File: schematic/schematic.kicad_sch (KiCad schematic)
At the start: 9 parts, among them J2 Conn_01x06, SW1 SW_SPDT, U1 ATmega88A-P, U2 SST39SF010, U3 74HC595, U4 74HC595

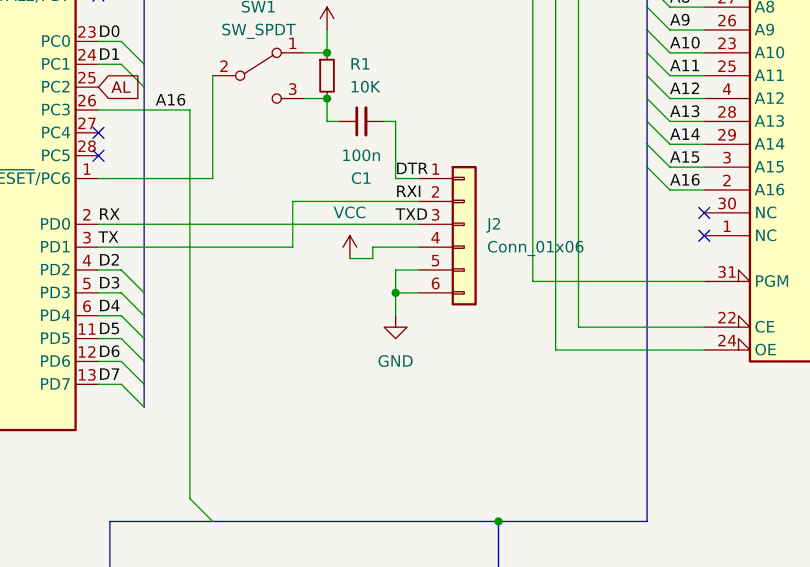
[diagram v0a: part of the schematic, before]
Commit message: finish readme, edit wires on header
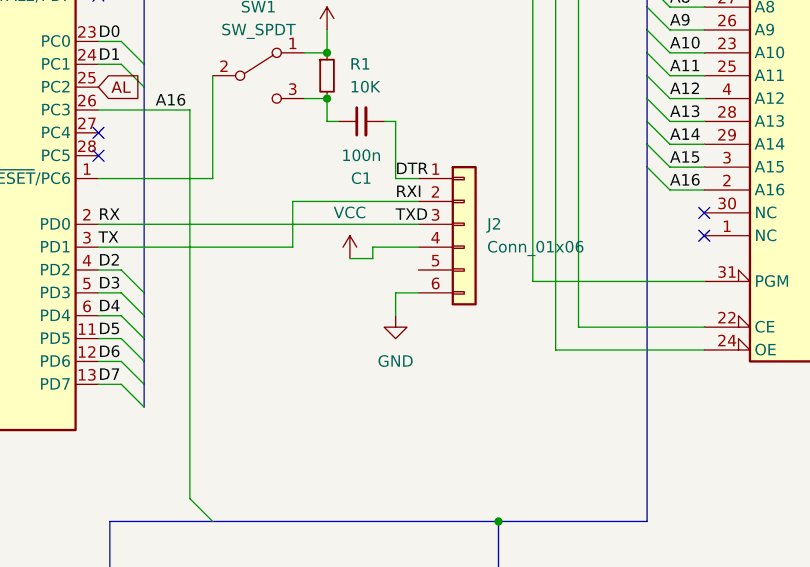
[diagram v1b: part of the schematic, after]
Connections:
- net GND: no longer J2.5 (Pin_5)
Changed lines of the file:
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@@
 (kicad_sch (version 20230121) (generator eeschema)
   (paper "A4")
-  (junction (at 135.89 99.06) (diameter 0) (color 0 0 0 0)
-  )
   (junction (at 128.27 77.47) (diameter 0) (color 0 0 0 0)
   )
@@
     (stroke (width 0) (type default))
   )
-  (wire (pts (xy 138.43 96.52) (xy 135.89 96.52))
-    (stroke (width 0) (type default))
-  )
   (wire (pts (xy 166.37 67.31) (xy 170.18 67.31))
     (stroke (width 0) (type default))
@@
     (stroke (width 0) (type default))
   )
-  (wire (pts (xy 135.89 96.52) (xy 135.89 99.06))
-    (stroke (width 0) (type default))
-  )
